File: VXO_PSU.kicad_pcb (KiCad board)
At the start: 4 copper layers, 210.2 x 40 mm, 52 parts, among them CON1 BARREL_JACK, P1 CONN_01X02, P10 CONN_02X08, P12 BNC, P13 BNC, P2 CONN_02X08, P3 CONN_02X08, P4 CONN_02X08, P5 CONN_02X08, P6 CONN_02X08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

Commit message: six layers
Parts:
- P2: moved to F.Cu
- turned P2 to 270 degrees
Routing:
- net -12V: track 0.00 -> 2.55 mm
- added copper zone on In4.Cu, net +12V
- added copper zone on In3.Cu, net -12V
- removed copper zone on In1.Cu, net +12V
- removed copper zone on In1.Cu, net -12V
- removed copper zone on In2.Cu, net -12V
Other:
- copper layers 4 -> 6

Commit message: tweak. ready to order probably
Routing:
- net /CV: track 134.3 -> 0.00 mm
- net /GATE: track 134.3 -> 0.16 mm
- net GND: track 3.75 -> 25.5 mm, vias 1 -> 16
- added copper zone on F.Cu, net /CV
- added copper zone on F.Cu, net /GATE
- added copper zone on B.Cu, net Net-(CON1-Pad1)
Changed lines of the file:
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@@
   (general
     (links 214)
-    (no_connects 0)
-    (area 27.174999 70.434999 262.382144 118.545)
+    (no_connects 17)
+    (area 27.174999 76.924999 237.575001 117.075001)
     (thickness 1.6)
     (drawings 19)
-    (tracks 40)
+    (tracks 38)
     (zones 0)
     (modules 52)
@@
   (page A4)
   (layers
-    (0 F.Cu signal hide)
-    (1 In1.Cu signal hide)
-    (2 In2.Cu signal hide)
+    (0 F.Cu signal)
+    (1 In1.Cu signal)
+    (2 In2.Cu signal)
     (3 In3.Cu signal)
-    (4 In4.Cu signal hide)
-    (31 B.Cu signal hide)
+    (4 In4.Cu signal)
+    (31 B.Cu signal)
     (32 B.Adhes user)
     (33 F.Adhes user)
@@
     (user_trace_width 1)
     (trace_clearance 0.25)
-    (zone_clearance 0.25)
+    (zone_clearance 0.3)
     (zone_45_only no)
     (trace_min 0.2)
@@
   (gr_line (start 237.5 77) (end 237.5 117) (angle 90) (layer Edge.Cuts) (width 0.15))
   (gr_line (start 27.25 77) (end 237.5 77) (angle 90) (layer Edge.Cuts) (width 0.15))
+  (segment (start 50.4 101.7) (end 51.5 101.7) (width 0.35) (layer B.Cu) (net 1))
+  (via (at 51.5 101.7) (size 1) (drill 0.5) (layers F.Cu B.Cu) (net 1))
+  (segment (start 49.3 101.7) (end 50.4 101.7) (width 0.35) (layer F.Cu) (net 1))
+  (via (at 50.4 101.7) (size 1) (drill 0.5) (layers F.Cu B.Cu) (net 1))
+  (segment (start 48.2 101.7) (end 49.3 101.7) (width 0.35) (layer B.Cu) (net 1))
+  (via (at 49.3 101.7) (size 1) (drill 0.5) (layers F.Cu B.Cu) (net 1))
+  (segment (start 46.75 101.75) (end 48.15 101.75) (width 0.35) (layer F.Cu) (net 1))
+  (segment (start 48.15 101.75) (end 48.2 101.7) (width 0.35) (layer F.Cu) (net 1))
+  (via (at 48.2 101.7) (size 1) (drill 0.5) (layers F.Cu B.Cu) (net 1))
+  (segment (start 46.5 112.75) (end 47.25 112.75) (width 0.35) (layer F.Cu) (net 1))
+  (segment (start 47.25 112.75) (end 47.8 112.2) (width 0.35) (layer F.Cu) (net 1))
+  (via (at 47.8 112.2) (size 1) (drill 0.5) (layers F.Cu B.Cu) (net 1))
+  (segment (start 85.2 93.2) (end 82.9 93.2) (width 0.35) (layer F.Cu) (net 1))
+  (via (at 82.9 93.2) (size 1) (drill 0.5) (layers F.Cu B.Cu) (net 1))
+  (segment (start 84 93.2) (end 85.2 93.2) (width 0.35) (layer B.Cu) (net 1))
+  (via (at 85.2 93.2) (size 1) (drill 0.5) (layers F.Cu B.Cu) (net 1))
+  (segment (start 84 91.75) (end 84 93.2) (width 0.35) (layer F.Cu) (net 1))
+  (via (at 84 93.2) (size 1) (drill 0.5) (layers F.Cu B.Cu) (net 1))
+  (segment (start 69 104.3) (end 69 105.4) (width 0.35) (layer F.Cu) (net 1))
+  (via (at 69 105.4) (size 1) (drill 0.5) (layers F.Cu B.Cu) (net 1))
+  (segment (start 69 103.2) (end 69 104.3) (width 0.35) (layer B.Cu) (net 1))
+  (via (at 69 104.3) (size 1) (drill 0.5) (layers F.Cu B.Cu) (net 1))
+  (segment (start 69 101.75) (end 69 103.2) (width 0.35) (layer F.Cu) (net 1))
+  (via (at 69 103.2) (size 1) (drill 0.5) (layers F.Cu B.Cu) (net 1))
+  (segment (start 65 94.5) (end 66.8 94.5) (width 0.35) (layer F.Cu) (net 1))
+  (via (at 66.8 94.5) (size 1) (drill 0.5) (layers F.Cu B.Cu) (net 1))
+  (segment (start 63.2 94.5) (end 65 94.5) (width 0.35) (layer B.Cu) (net 1))
+  (via (at 65 94.5) (size 1) (drill 0.5) (layers F.Cu B.Cu) (net 1))
+  (segment (start 63.25 92.75) (end 63.25 94.45) (width 0.35) (layer F.Cu) (net 1))
+  (segment (start 63.25 94.45) (end 63.2 94.5) (width 0.35) (layer F.Cu) (net 1))
+  (via (at 63.2 94.5) (size 1) (drill 0.5) (layers F.Cu B.Cu) (net 1))
+  (segment (start 69 93.25) (end 69 91.8) (width 0.35) (layer F.Cu) (net 1))
+  (via (at 69 91.8) (size 1) (drill 0.5) (layers F.Cu B.Cu) (net 1))
   (segment (start 45 112.75) (end 45 110.5) (width 0.35) (layer F.Cu) (net 1))
   (segment (start 45 112.75) (end 46.5 112.75) (width 0.35) (layer F.Cu) (net 1))
   (via (at 46.5 112.75) (size 1) (drill 0.5) (layers F.Cu B.Cu) (net 1))
   (segment (start 64.54 78.75) (end 64.54 81.3) (width 1.8) (layer In3.Cu) (net 7))
-  (segment (start 76.6 103.2) (end 74.06 103.2) (width 0.35) (layer F.Cu) (net 11))
-  (segment (start 90.73 103.35) (end 76.65 103.35) (width 0.35) (layer F.Cu) (net 11))
-  (segment (start 76.65 103.35) (end 76.54 103.24) (width 0.35) (layer F.Cu) (net 11))
-  (segment (start 93.27 103.35) (end 90.73 103.35) (width 0.35) (layer F.Cu) (net 11))
-  (segment (start 106.73 103.35) (end 93.27 103.35) (width 0.35) (layer F.Cu) (net 11))
-  (segment (start 109.27 103.35) (end 106.73 103.35) (width 0.35) (layer F.Cu) (net 11))
-  (segment (start 122.73 103.35) (end 109.27 103.35) (width 0.35) (layer F.Cu) (net 11))
-  (segment (start 125.27 103.35) (end 122.73 103.35) (width 0.35) (layer F.Cu) (net 11))
-  (segment (start 139.73 103.35) (end 125.27 103.35) (width 0.35) (layer F.Cu) (net 11))
-  (segment (start 142.27 103.35) (end 139.73 103.35) (width 0.35) (layer F.Cu) (net 11))
-  (segment (start 156.73 103.35) (end 142.27 103.35) (width 0.35) (layer F.Cu) (net 11))
-  (segment (start 159.27 103.35) (end 156.73 103.35) (width 0.35) (layer F.Cu) (net 11))
-  (segment (start 173.73 103.35) (end 159.27 103.35) (width 0.35) (layer F.Cu) (net 11))
-  (segment (start 176.27 103.35) (end 173.73 103.35) (width 0.35) (layer F.Cu) (net 11))
-  (segment (start 189.73 103.35) (end 176.27 103.35) (width 0.35) (layer F.Cu) (net 11))
-  (segment (start 192.27 103.35) (end 189.73 103.35) (width 0.35) (layer F.Cu) (net 11))
-  (segment (start 205.73 103.35) (end 192.27 103.35) (width 0.35) (layer F.Cu) (net 11))
-  (segment (start 208.27 103.35) (end 205.73 103.35) (width 0.35) (layer F.Cu) (net 11))
-  (segment (start 76.54 105.78) (end 90.62 105.78) (width 0.35) (layer F.Cu) (net 12))
-  (segment (start 74 105.78) (end 76.54 105.78) (width 0.35) (layer F.Cu) (net 12))
-  (segment (start 125.27 105.89) (end 139.73 105.89) (width 0.35) (layer F.Cu) (net 12))
-  (segment (start 122.73 105.89) (end 125.27 105.89) (width 0.35) (layer F.Cu) (net 12))
-  (segment (start 109.27 105.89) (end 122.73 105.89) (width 0.35) (layer F.Cu) (net 12))
-  (segment (start 205.73 105.89) (end 208.27 105.89) (width 0.35) (layer F.Cu) (net 12))
-  (segment (start 192.27 105.89) (end 205.73 105.89) (width 0.35) (layer F.Cu) (net 12))
-  (segment (start 189.73 105.89) (end 192.27 105.89) (width 0.35) (layer F.Cu) (net 12))
-  (segment (start 176.27 105.89) (end 189.73 105.89) (width 0.35) (layer F.Cu) (net 12))
-  (segment (start 173.73 105.89) (end 176.27 105.89) (width 0.35) (layer F.Cu) (net 12))
-  (segment (start 159.27 105.89) (end 173.73 105.89) (width 0.35) (layer F.Cu) (net 12))
-  (segment (start 156.73 105.89) (end 159.27 105.89) (width 0.35) (layer F.Cu) (net 12))
-  (segment (start 142.27 105.89) (end 156.73 105.89) (width 0.35) (layer F.Cu) (net 12))
-  (segment (start 139.73 105.89) (end 142.27 105.89) (width 0.35) (layer F.Cu) (net 12))
-  (segment (start 106.73 105.89) (end 109.27 105.89) (width 0.35) (layer F.Cu) (net 12))
-  (segment (start 93.27 105.89) (end 106.73 105.89) (width 0.35) (layer F.Cu) (net 12))
-  (segment (start 90.73 105.89) (end 93.27 105.89) (width 0.35) (layer F.Cu) (net 12))
   (segment (start 90.62 105.78) (end 90.73 105.89) (width 0.35) (layer F.Cu) (net 12))
   (zone (net 1) (net_name GND) (layer F.Cu) (hatch edge 0.508)
@@
       )
     )
+  )
+  (zone (net 9) (net_name "Net-(CON1-Pad1)") (layer B.Cu) (hatch edge 0.508)
+    (priority 1)
+    (connect_pads yes (clearance 0.3))
+    (min_thickness 0.254)
+    (fill yes (arc_segments 16) (thermal_gap 0.508) (thermal_bridge_width 0.508))
+    (polygon
+      (pts
+        (xy 54.739779 78.5) (xy 54.739779 86.25) (xy 43.989779 86.25) (xy 43.989779 80.5) (xy 49.989779 80.5)
+        (xy 49.989779 78.5)
+      )
+    )
+  )
+  (zone (net 11) (net_name /CV) (layer F.Cu) (hatch edge 0.508)
+    (priority 1)
+    (connect_pads yes (clearance 0.3))
+    (min_thickness 0.254)
+    (fill yes (arc_segments 16) (thermal_gap 0.508) (thermal_bridge_width 0.508))
+    (polygon
+      (pts
+        (xy 74.2 102.9) (xy 208.8 102.9) (xy 208.8 103.8) (xy 74.2 103.8)
+      )
+    )
+  )
+  (zone (net 12) (net_name /GATE) (layer F.Cu) (hatch edge 0.508)
+    (priority 1)
+    (connect_pads yes (clearance 0.3))
+    (min_thickness 0.254)
+    (fill yes (arc_segments 16) (thermal_gap 0.508) (thermal_bridge_width 0.508))
+    (polygon
+      (pts
+        (xy 74.228514 105.4354) (xy 208.828514 105.4354) (xy 208.828514 106.3354) (xy 74.228514 106.3354)
+      )
+    )

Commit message: fiddly tricks
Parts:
- moved U2 1.50 mm to (62.0, 80.2)
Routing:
- net +12V: track 0.00 -> 5.90 mm
- removed copper zone on In2.Cu, net +12V

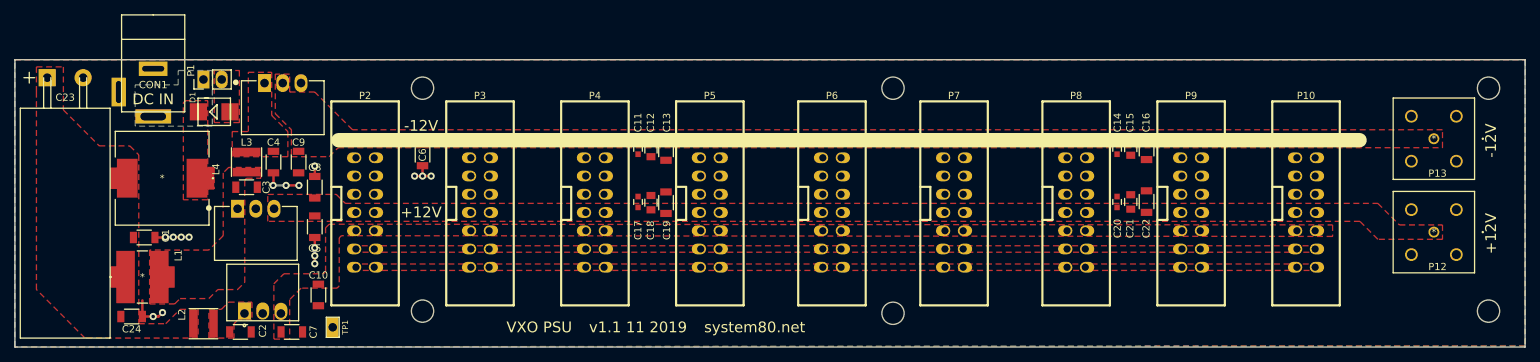
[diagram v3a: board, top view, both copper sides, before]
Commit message: this commit reverts back to 4layer. boards ordered
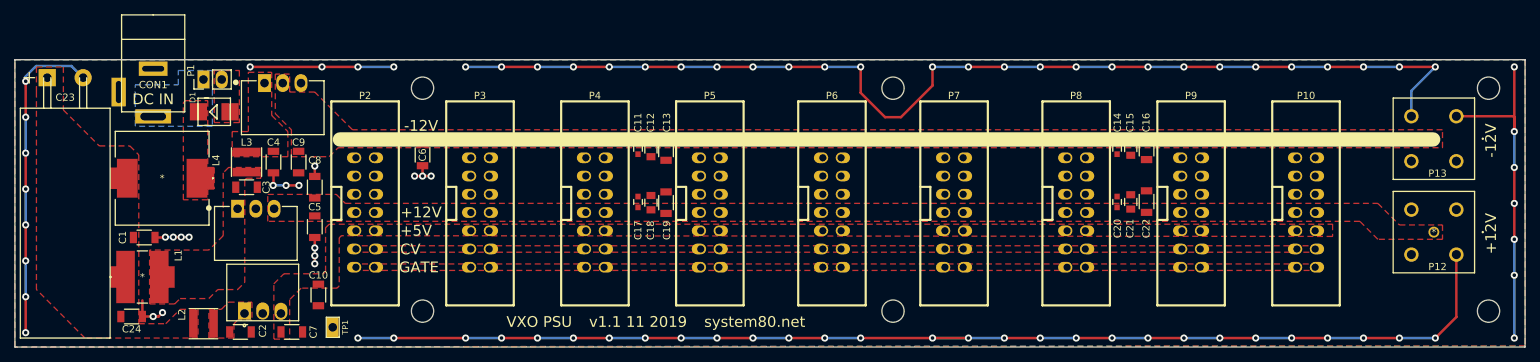
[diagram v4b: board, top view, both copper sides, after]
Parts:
- moved HOLE-M3 0.24 mm to (84.0, 81.0)
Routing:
- net GND: track 25.5 -> 463.0 mm, vias 16 -> 91
- added copper zone on In1.Cu, net +12V
- added copper zone on In1.Cu, net -12V
- removed copper zone on In4.Cu, net +12V
- removed copper zone on In3.Cu, net -12V
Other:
- copper layers 6 -> 4
- board text added: "+5V"
- board text added: "CV"
- board text added: "GATE"
